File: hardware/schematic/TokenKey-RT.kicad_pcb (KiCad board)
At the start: 4 copper layers, 50 x 40 mm, 103 parts, among them J1 USB-C, J2 Header 1x04 P2.54 H3.0 (OLED), J3 TC2030-NL, Q1 AO3401A, SW1 SW_BOOT, SW2 EC11E18244A5, SW3 BTN1, SW4 BTN2, U1 MIMXRT1062DVL6B, U2 AP2112K-3.3TRG1, U3 TLV62569DBVR, U4 W25Q64JVSSIQ, U5 APS6404L-3SQR-ZR, U6 USBLC6-2SC6, Y1 24MHz 12pF, Y2 32.768kHz 12.5pF

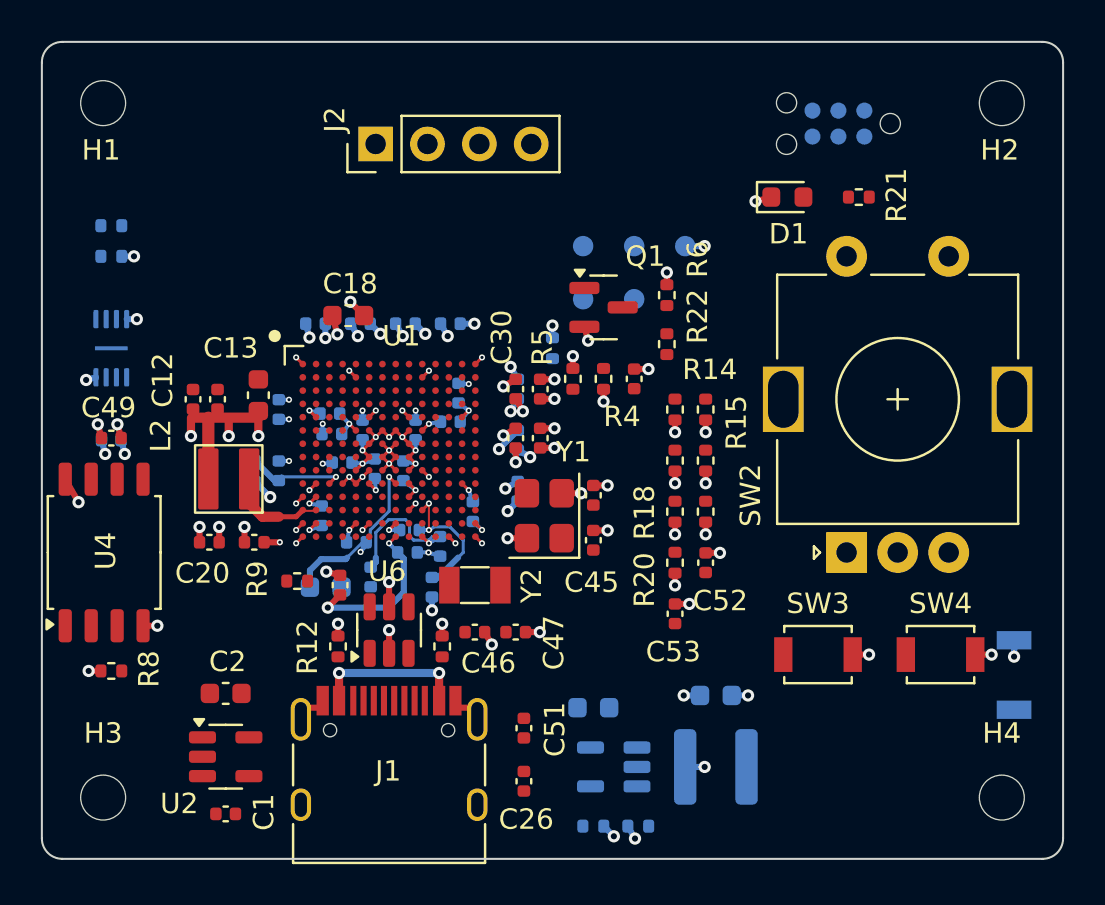
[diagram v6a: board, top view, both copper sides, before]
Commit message: Routing phase 1: power entry (VBUS, LDO, spare buck) and plane vias
VBUS: J1 vias to a 0.40 mm B.Cu trunk. West: B.Cu to a via at (6.7, 33.3),
F.Cu rail west of U2 to U2.1/U2.3 and C1.1. East: B.Cu to C51/C26 (F.Cu
via at 24.4, 34.5), C3.1 and U3.1; U3.1-U3.4 (VIN/EN) under the U3 body.
VBUS sense: U6.5 and ball N6 tied on In2 by a 0.30 mm VBUS track
(N6 via - U6.5 via - J1 east VBUS via); the 3V3 plane flows around it.
U2.5 (3V3 out) to C2.1 plus three 3V3 plane vias. Spare buck (DNP):
BUCK_SW 0.50 mm on B.Cu south of L1.2 (far from Y1/Y2), BUCK_FB 0.20 mm.
Own GND via for C1, C2, U2, C51, C26, C3, U3, J3.5, C11, C12, C13; 3V3 via
for J3.1. C40.2/C42.2 tied on B.Cu to the C22 GND via.

Hand edit (pcbnew script, collision-checked; grid search for the short
B.Cu/In2 legs). Zones refilled.

Part of #57
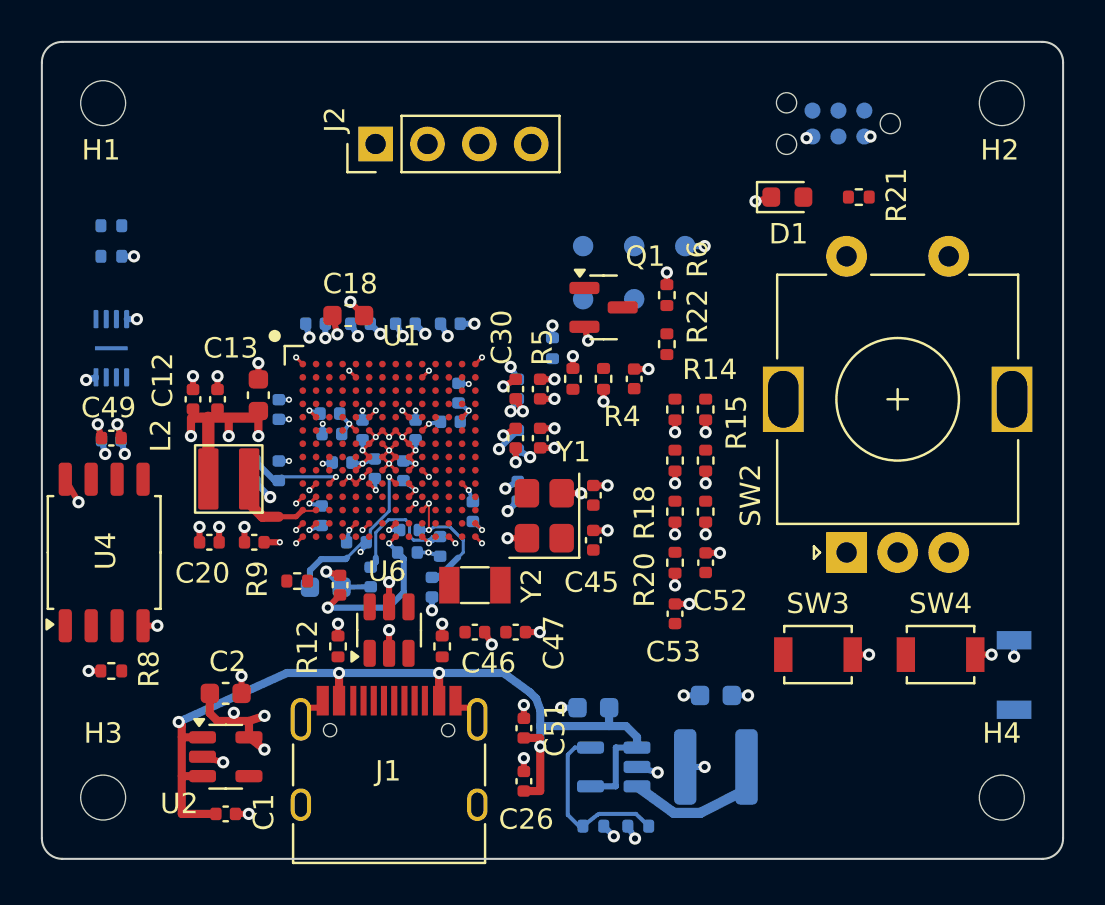
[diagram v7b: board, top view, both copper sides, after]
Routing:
- net VBUS: track 9.29 -> 55.8 mm, vias 4 -> 6
- net GND: track 54.0 -> 64.6 mm, vias 66 -> 77
- net BUCK_FB: track 0.00 -> 8.84 mm
- net BUCK_SW: track 0.00 -> 7.16 mm
- net 3V3: track 34.7 -> 41.1 mm, vias 48 -> 52

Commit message: Routing phase 1: GND stitching, outer GND pours, cleanup
GND pours on F.Cu and B.Cu (GND_POUR_TOP/BOT: 0.30 mm clearance, 0.20 mm
min width, solid SMD / thermal THT, islands removed) with a NO_POUR_U1 rule
area over the BGA and its bottom decoupling (x 11.2-22.8, y 13-25.8) so the
pour does not starve the 0402 thermals or fill the escape channels.
61 GND stitching vias (0.6/0.3): ring 0.95 mm in from the board edge at
about 2.5 mm pitch (skipping the H1-H4 keepouts, J3 rule area and parts),
plus three beside the J1 shell. Removed two single-layer vias left from
c955b6a (VDD_SNVS_CAP 18.95,22.6; VDD_USB_CAP 15.605,24.976).

Result: DRC 0 errors, 20 warnings (pre-existing silk/lib); 0 unconnected on
power/GND nets; 69 signal unconnected left for phases 2-4; schematic parity
clean. Hand edit (pcbnew script). Zones refilled.

Fixes #57
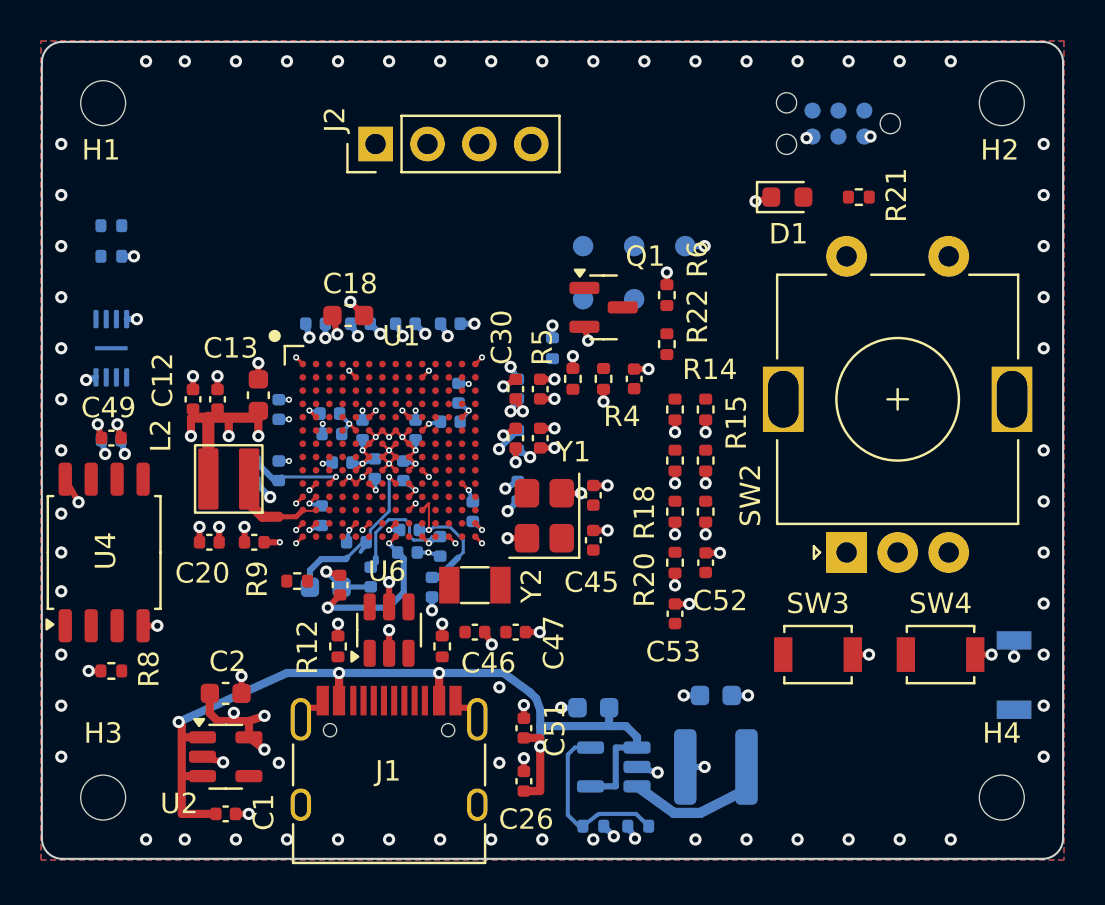
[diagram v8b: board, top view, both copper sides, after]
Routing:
- net VDD_USB_CAP: vias 2 -> 1
- net VDD_SNVS_CAP: vias 2 -> 1
- net GND: vias 77 -> 138
- added copper zone on B.Cu, net GND
- added copper zone on F.Cu, net GND
